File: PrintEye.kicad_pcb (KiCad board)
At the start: 2 copper layers, 18 parts, among them J1 FTDI, J2 Pause Button, J3 Activity LED, Q1 2N7000, Q2 2N7000, U1 ATmega328-PU, Y1 16MHz

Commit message: PCB design and footprints
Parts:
- OLED1, OLED2: value SH1106_I2C_OLED -> SSD1315_I2C_OLED; footprint Connector_PinSocket_1.27mm:PinSocket_1x04_P1.27mm_Vertical -> PrintEyeHardware:SSD1315-I2C-OLED
- Q1, Q2: footprint Package_TO_SOT_THT:TO-92_Inline -> Package_TO_SOT_THT:TO-92_Inline_Wide
- Y1: footprint Crystal:Crystal_HC50_Vertical -> Crystal:Crystal_HC49-4H_Vertical
- moved R5 50.1 mm to (121.9, 100.3), turned to 0 degrees
- moved R4 45.5 mm to (121.9, 104.1), turned to 0 degrees
- moved R2 45.1 mm to (121.9, 108.0), turned to 0 degrees
- moved J1 44.9 mm to (168.9, 114.9), turned to 180 degrees
- moved R1 42.1 mm to (129.5, 115.6), turned to 180 degrees
- moved OLED2 41.5 mm to (133.3, 90.2), turned to 180 degrees
- moved R3 36.4 mm to (131.4, 111.8), turned to 180 degrees
- moved C5 32.5 mm to (132.1, 114.9), turned to 0 degrees
- moved C2 28.7 mm to (165.7, 109.2), turned to 180 degrees
- moved U1 28.3 mm to (133.3, 105.4), turned to 90 degrees
- moved J3 25.1 mm to (168.9, 95.2)
- moved Q1 24.9 mm to (137.8, 111.8), turned to 135 degrees
- moved OLED1 23.5 mm to (158.8, 90.2), turned to 180 degrees
- moved J2 23.2 mm to (168.9, 92.1), turned to 180 degrees
- moved Q2 15.8 mm to (143.5, 111.8), turned to 135 degrees
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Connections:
- net SCL1 renamed SCK1
- net SCL2 renamed SCK2
- J1 pad 5: (no net) -> Net-(J1-Pad5)
- OLED1 pad 1: 5v -> GND
- OLED1 pad 2: GND -> 5v
- OLED2 pad 1: 5v -> GND
- OLED2 pad 2: GND -> 5v
- U1 pad 11: (no net) -> Net-(U1-Pad11)
- U1 pad 12: (no net) -> Net-(U1-Pad12)
- U1 pad 13: (no net) -> Net-(U1-Pad13)
- U1 pad 14: (no net) -> Net-(U1-Pad14)
- U1 pad 17: (no net) -> Net-(U1-Pad17)
- U1 pad 18: (no net) -> Net-(U1-Pad18)
- U1 pad 19: (no net) -> Net-(U1-Pad19)
- U1 pad 21: (no net) -> Net-(U1-Pad21)
- U1 pad 23: (no net) -> Net-(U1-Pad23)
- U1 pad 24: (no net) -> Net-(U1-Pad24)
- U1 pad 4: (no net) -> Net-(U1-Pad4)
- U1 pad 5: (no net) -> Net-(U1-Pad5)
- U1 pad 6: (no net) -> Net-(U1-Pad6)
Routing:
- net 5v: track 185.5 -> 132.0 mm
- net Net-(C5-Pad1): track 42.1 -> 18.4 mm
- net RX: track 33.4 -> 12.6 mm
- net GND: track 0.00 -> 19.2 mm, vias 0 -> 4
- net RTS: track 18.2 -> 34.8 mm
- net TX: track 29.9 -> 15.8 mm
- net 3v3: track 28.1 -> 15.6 mm
- net RX-3v3: track 20.1 -> 31.0 mm
- net SCK2: track 16.2 -> 6.88 mm
- net TX-3v3: track 17.0 -> 25.7 mm
- net SDA2: track 14.6 -> 6.88 mm
- net Net-(C1-Pad2): track 14.9 -> 7.94 mm
- net Net-(J2-Pad2): track 2.98 -> 9.67 mm
- net Net-(R6-Pad1): track 2.59 -> 9.23 mm
- net Net-(C2-Pad2): track 15.3 -> 9.98 mm
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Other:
- board outline added: 52.1 x 29.8 mm
- net class Default: clearance 0.2 -> 0.3; trace_width 0.25 -> 0.8
- rule trace_clearance: 0.2 -> 0.3
- board text added: "By Owen"
- board text added: "PrintEye"
- board text added: "printEYE"

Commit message: Swap TX and RX..
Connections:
- J1 pad 2: RX-3v3 -> TX-3v3
- J1 pad 3: TX-3v3 -> RX-3v3
- J1 pad 5: Net-(J1-Pad5) -> (no net)
- U1 pad 11: Net-(U1-Pad11) -> (no net)
- U1 pad 12: Net-(U1-Pad12) -> (no net)
- U1 pad 13: Net-(U1-Pad13) -> (no net)
- U1 pad 14: Net-(U1-Pad14) -> (no net)
- U1 pad 17: Net-(U1-Pad17) -> (no net)
- U1 pad 18: Net-(U1-Pad18) -> (no net)
- U1 pad 19: Net-(U1-Pad19) -> (no net)
- U1 pad 21: Net-(U1-Pad21) -> (no net)
- U1 pad 23: Net-(U1-Pad23) -> (no net)
- U1 pad 24: Net-(U1-Pad24) -> (no net)
- U1 pad 4: Net-(U1-Pad4) -> (no net)
- U1 pad 5: Net-(U1-Pad5) -> (no net)
- U1 pad 6: Net-(U1-Pad6) -> (no net)
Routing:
- net RX-3v3: track 31.0 -> 32.6 mm, vias 0 -> 2
- net TX-3v3: track 25.7 -> 27.3 mm
- net RTS: track 34.8 -> 35.6 mm

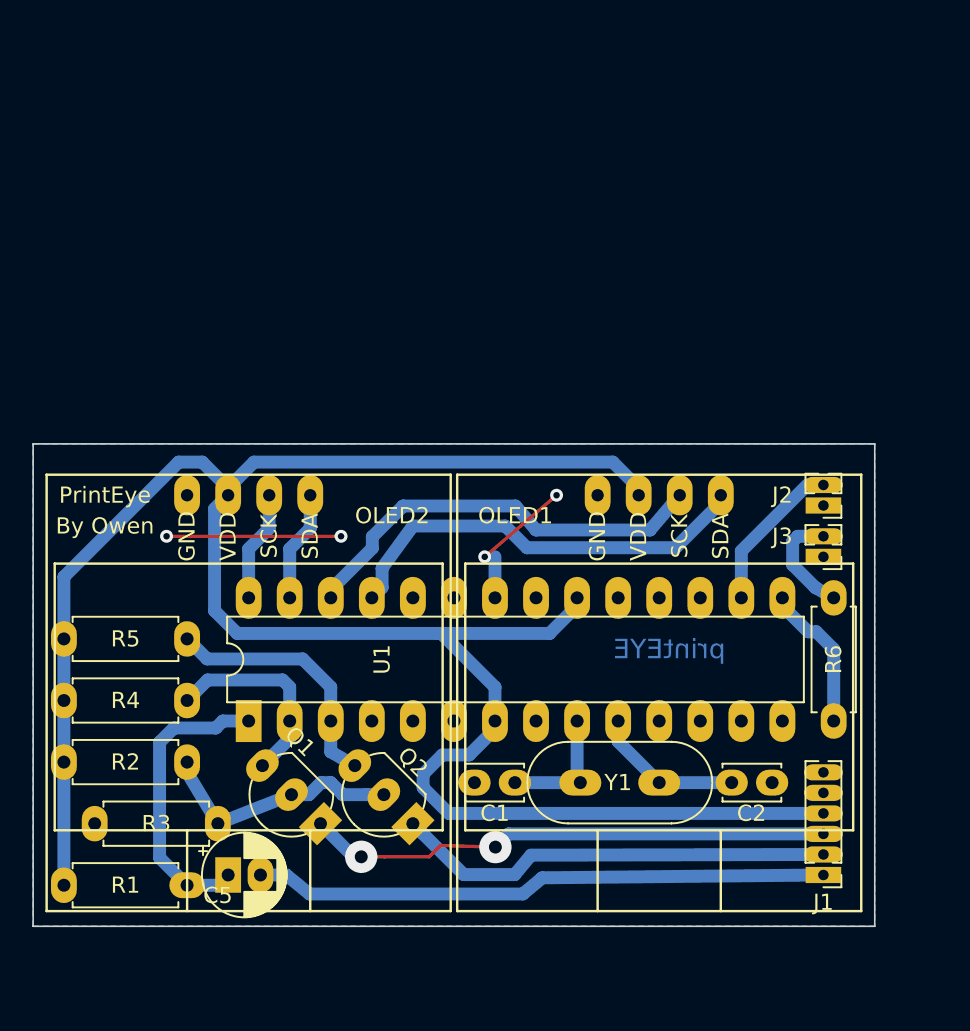
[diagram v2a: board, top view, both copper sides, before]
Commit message: Move to a bigger connector size
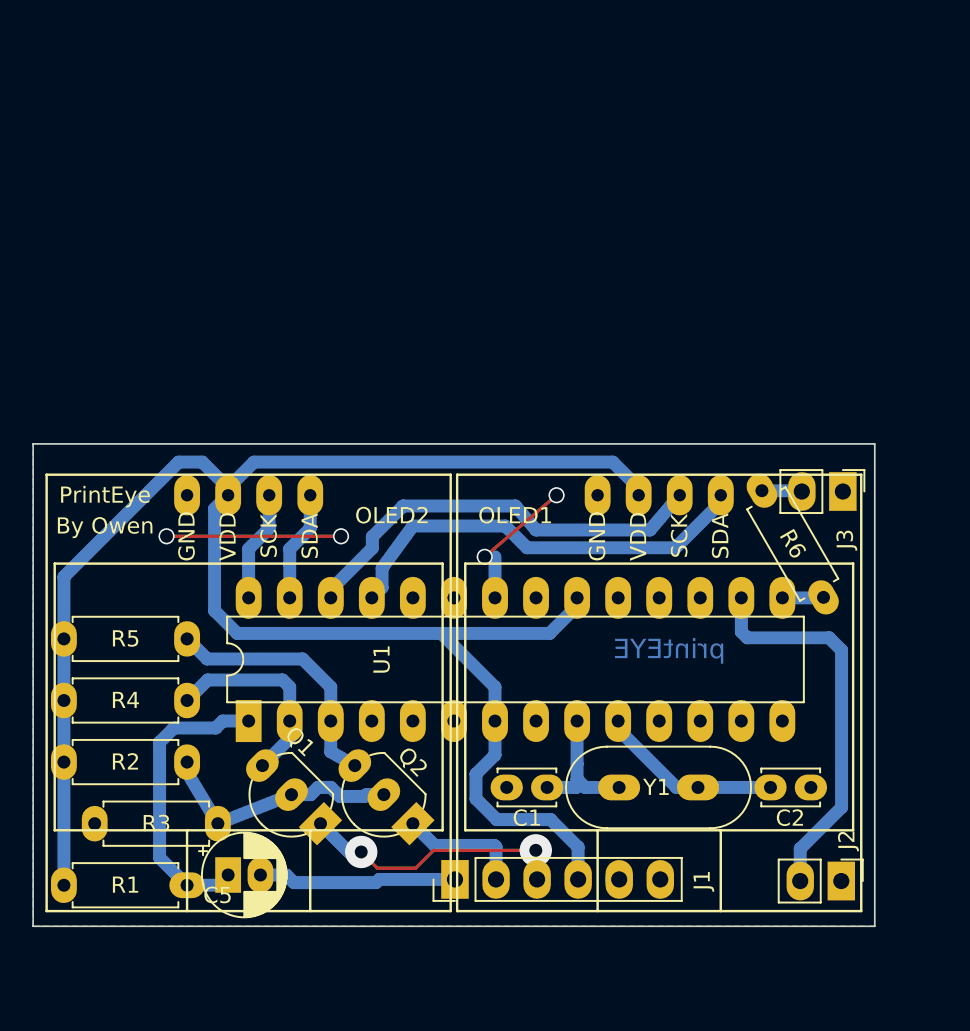
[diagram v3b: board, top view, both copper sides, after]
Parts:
- J1: footprint Connector_PinHeader_1.27mm:PinHeader_1x06_P1.27mm_Vertical -> Connector_PinHeader_2.54mm:PinHeader_1x06_P2.54mm_Vertical
- J2, J3: footprint Connector_PinHeader_1.27mm:PinHeader_1x02_P1.27mm_Vertical -> Connector_PinHeader_2.54mm:PinHeader_1x02_P2.54mm_Vertical
- moved J2 23.3 mm to (170.0, 115.3), turned to 270 degrees
- moved J1 22.8 mm to (146.1, 115.2), turned to 90 degrees
- moved R6 7.68 mm to (168.9, 97.8), turned to 120 degrees
- moved J3 4.22 mm to (170.1, 91.2), turned to 270 degrees
- moved Y1 2.42 mm to (161.2, 109.5)
- moved C2 2.42 mm to (168.1, 109.5)
- moved C1 2.02 mm to (149.3, 109.5)
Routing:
- net RTS: track 35.6 -> 12.3 mm
- net TX-3v3: track 27.3 -> 7.75 mm
- net 5v: track 132.0 -> 115.1 mm
- net RX-3v3: track 32.6 -> 16.7 mm
- net Net-(J2-Pad2): track 9.67 -> 24.1 mm
- net Net-(R6-Pad1): track 9.23 -> 2.56 mm
- net Net-(J3-Pad2): track 6.78 -> 2.49 mm
- net Net-(C2-Pad2): track 9.98 -> 11.4 mm
- net Net-(C1-Pad2): track 7.94 -> 8.74 mm
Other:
- net class Default: clearance 0.3 -> 0.5
- rule trace_clearance: 0.3 -> 0.5
